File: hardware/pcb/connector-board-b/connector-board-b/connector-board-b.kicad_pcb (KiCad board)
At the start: 2 copper layers, 27.4 x 70.6 mm, 46 parts, among them J1 DE9_Pins, J2 PANEL_18V, J5 8-215570-0, J6 NTC_103AT, J7 BATTERY, Q1 Si4840BDY, Q2 Si4840BDY, SW1 PWR_KILL, U1 BQ24650RVA, U2 INA3221, U3 MCP1700-3.3

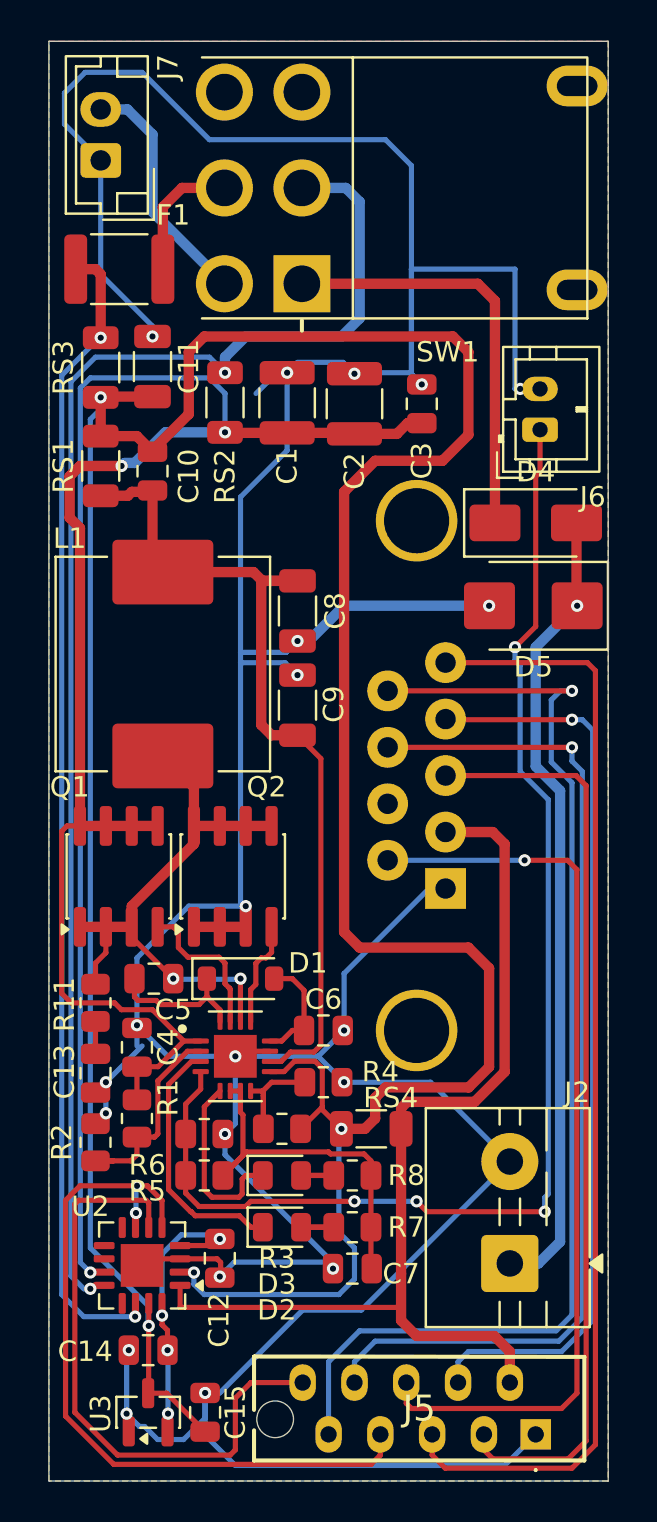
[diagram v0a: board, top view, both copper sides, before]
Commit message: Final PCB adjuments to rev 1.1
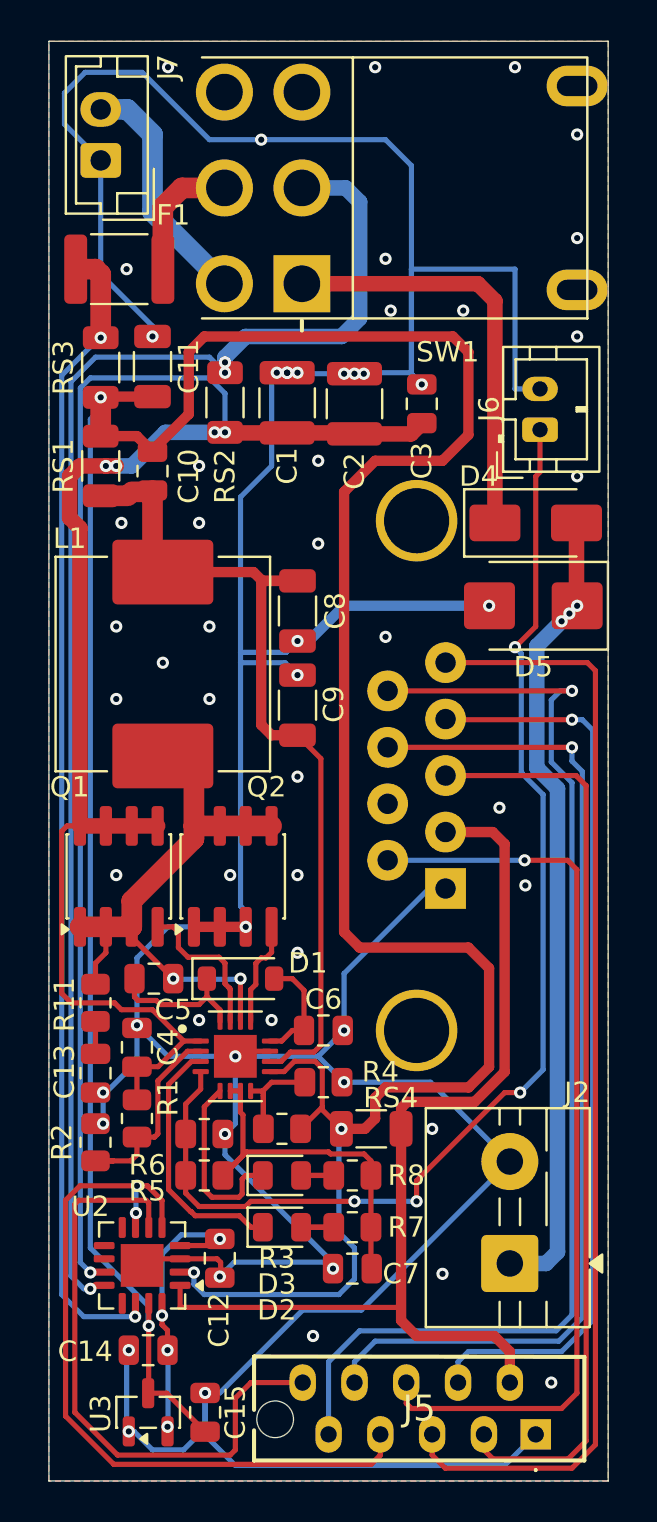
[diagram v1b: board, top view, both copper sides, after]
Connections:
- J1 pad SH: (no net) -> GND
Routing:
- net Net-(J6-Pin_1): track 64.1 -> 59.9 mm
- net GND: track 240.5 -> 239.2 mm, vias 21 -> 61
- net Net-(U1-PH): track 28.6 -> 29.5 mm
- net VIN: track 114.1 -> 114.0 mm, vias 3 -> 5
- net Net-(D4-A): track 39.5 -> 39.6 mm, vias 1 -> 3
- net PANEL+: vias 2 -> 3
